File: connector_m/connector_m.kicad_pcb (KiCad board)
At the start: 2 copper layers, 100 x 47.1 mm, 33 parts, among them J1 PowerOut, J2 PowerIn, J3 CANFD_In, U1 SKA2P1_TX, U2 TJA1042T, U3 SKA2P1_RX, U5 XC6206P182MR, U6 LSF0102DCUR

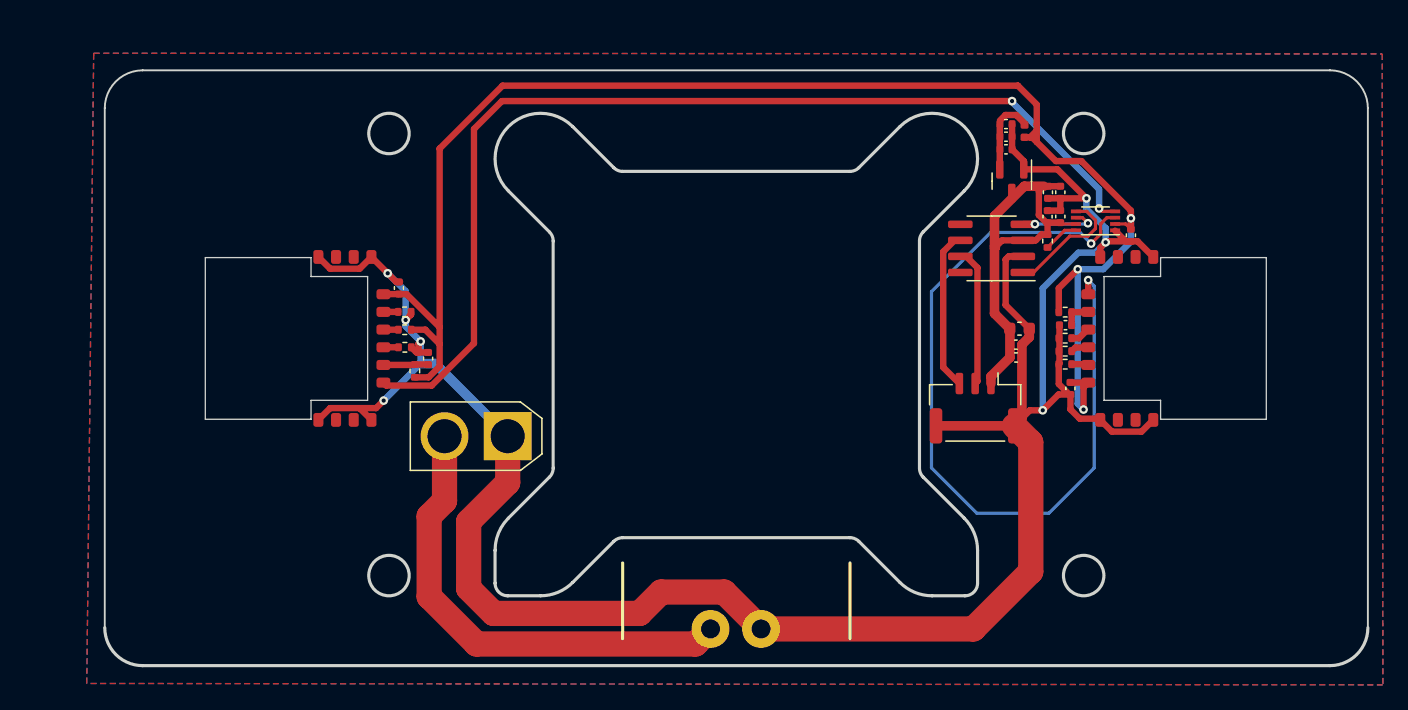
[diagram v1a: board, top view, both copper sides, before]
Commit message: [New] Re-layout PCB connector male
Signed-off-by: Homalozoa <nx.tardis@gmail.com>
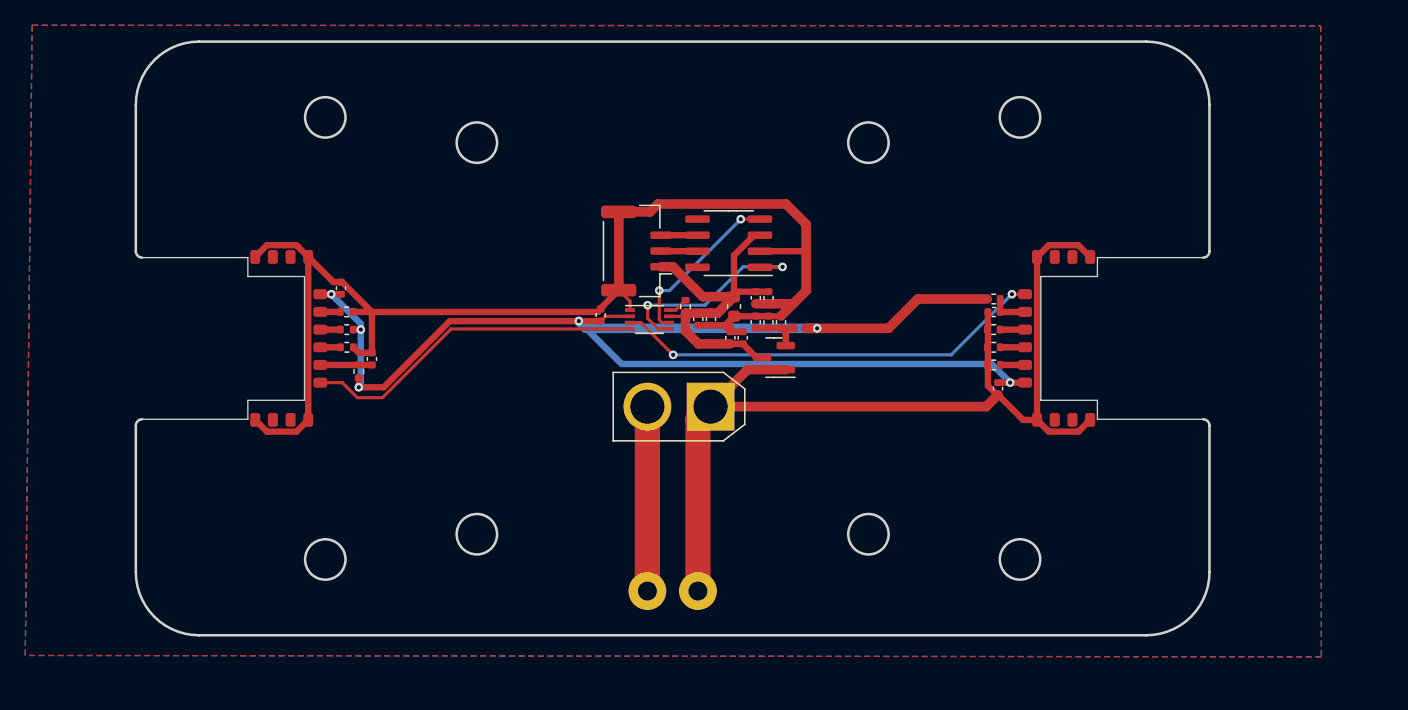
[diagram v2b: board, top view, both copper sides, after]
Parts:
- moved C13 42.5 mm to (94.3, 58.1), turned to 90 degrees
- moved U6 36.2 mm to (98.2, 58.5), turned to 0 degrees
- moved C23 29.8 mm to (102.0, 58.5), turned to -90 degrees
- moved J3 29.6 mm to (97.1, 53.1), turned to 90 degrees
- moved R12 29.1 mm to (101.0, 57.5), turned to -90 degrees
- moved C14 28.5 mm to (104.6, 60.0), turned to 90 degrees
- moved C21 27.9 mm to (103.0, 58.5), turned to -90 degrees
- moved C15 26.8 mm to (105.5, 60.0), turned to 90 degrees
- moved C17 25.3 mm to (106.6, 58.7), turned to 90 degrees
- moved C18 23.9 mm to (107.6, 58.7), turned to 90 degrees
- moved L2 23.7 mm to (110.1, 59.2), turned to 0 degrees
- moved U5 23.4 mm to (108.0, 61.5), turned to 180 degrees
- moved C8 22.7 mm to (104.9, 57.5), turned to -90 degrees
- moved C19 22.5 mm to (108.6, 58.7), turned to 90 degrees
- moved C4 21.1 mm to (106.6, 56.8), turned to -90 degrees
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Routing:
- net RX_1V8: track 81.9 -> 27.3 mm, vias 2 -> 0
- net TX_1V8: track 64.2 -> 34.3 mm
- net +24V: track 37.3 -> 14.6 mm
- net GND: track 198.4 -> 183.7 mm, vias 7 -> 0
- net +1V8: track 121.2 -> 107.9 mm, vias 3 -> 6
- net CANFD_L: track 12.7 -> 2.89 mm
- net CANFD_H: track 11.0 -> 2.89 mm
- net CANFD_RX: track 6.32 -> 13.5 mm
- net CANFD_TX: track 9.69 -> 16.8 mm, vias 0 -> 2
- net +5V: track 31.8 -> 29.8 mm
- net Net-(C17-Pad1): track 6.05 -> 4.55 mm
- net Net-(R12-Pad1): track 2.81 -> 1.62 mm
- net Net-(C7-Pad1): track 2.27 -> 3.02 mm
- net Net-(R6-Pad2): track 1.27 -> 1.97 mm
- net Net-(R8-Pad2): track 1.36 -> 1.97 mm
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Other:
- board size 100 x 47.1 mm -> 85 x 47 mm
